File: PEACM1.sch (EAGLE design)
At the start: 15 parts

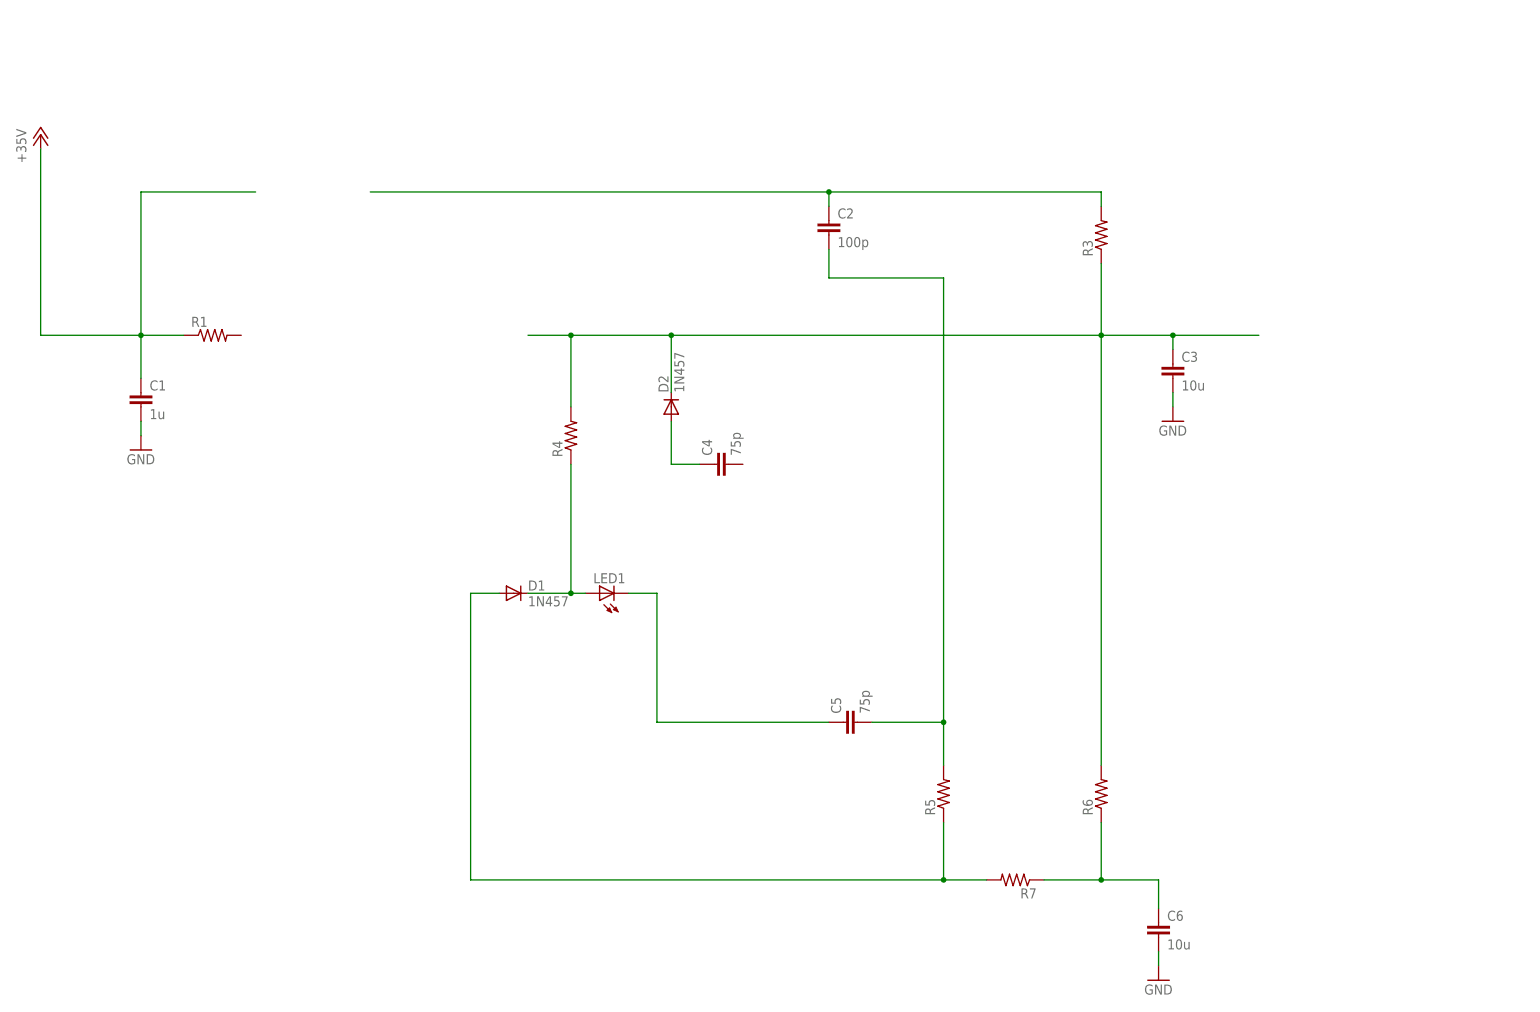
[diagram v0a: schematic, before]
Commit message: Schematic components from example complete. Needs connectors, V+ for OpAmp.
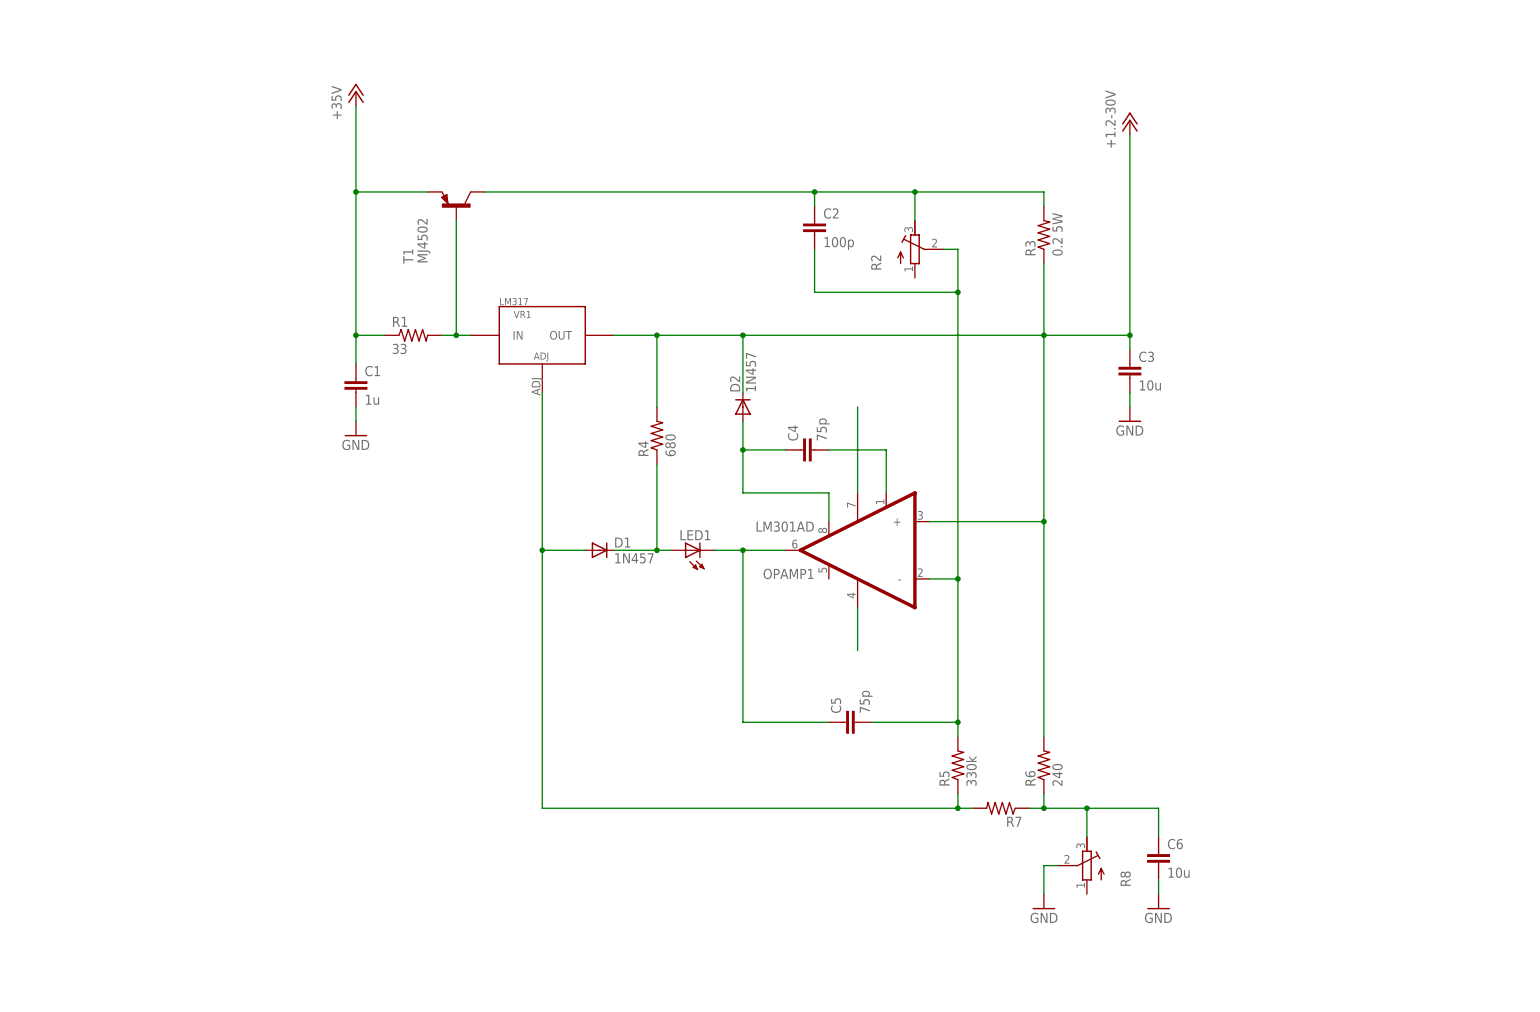
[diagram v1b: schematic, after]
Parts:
- added OPAMP1: LM301AD, PEAC:LM301AD
- added R2, R8: (no value), rcl:R-TRIMM4G/J
- added T1: MJ4502, transistor:-PNP-TO3
- added VR1: LM317, PEAC:LM317
- R1: value (none) -> 33
- R3: value (none) -> 0.2 5W; device rcl:R-US_M1206 -> rcl:R-US_R4527
- R4: value (none) -> 680
- R5: value (none) -> 330k
- R6: value (none) -> 240
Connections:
- new net +1.2-30V: C3.1, D2.C, OPAMP1.+@3, R3.1, R4.2, R6.2, VR1.OUT
- new net N$1: C4.2, OPAMP1.BAL#1
- new net VCC+@7: OPAMP1.VCC+@7
- new net VCC-@4: OPAMP1.VCC-@4
- net +35V: now also T1.E
- net GND: now also R8.S
- net N$11: now also OPAMP1.OUT_A@6
- net N$2: now also R2.E, T1.C
- net N$3: now also R1.2, T1.B, VR1.IN; no longer C3.1, D2.C, R3.1, R4.2, R6.2
- net N$4: now also OPAMP1.-@2, R2.S
- net N$5: now also VR1.ADJ
- net N$6: now also R8.E
- net N$9: now also OPAMP1.BAL@8
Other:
- moved on the sheet: C1, C2, C3, C4, C6, D1, D2, LED1, R1, R3, R4, R5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

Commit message: Schematic and layout ready for review.
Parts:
- added H1, H2: MOUNT-PAD-ROUND2.8, holes:MOUNT-PAD-ROUND2.8
- added JP1, JP2: (no value), pinhead:PINHD-1X2
- added R9: NU, rcl:R-US_M1206
- R7: value (none) -> 220
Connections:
- removed net VCC+@7: OPAMP1.VCC+@7
- removed net VCC-@4: OPAMP1.VCC-@4
- new net VCC-: OPAMP1.VCC-@4, R9.2
- net +1.2-30V: now also JP2.1
- net +35V: now also JP1.2, OPAMP1.VCC+@7
- net GND: now also H1.MOUNT, H2.MOUNT, JP1.1, JP2.2, R9.1
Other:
- moved on the sheet: C5, C6, R5, R6, R7, R8

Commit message: Completed board layout.
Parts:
- added JP3: (no value), pinhead:PINHD-1X2
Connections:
- net GND: now also JP3.1
- net VCC-: now also JP3.2
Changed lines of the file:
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@@
 <part name="H2" library="holes" deviceset="MOUNT-PAD-ROUND" device="2.8"/>
 <part name="GND8" library="PEAC" deviceset="GND" device=""/>
+<part name="JP3" library="pinhead" deviceset="PINHD-1X2" device=""/>
+<part name="GND9" library="PEAC" deviceset="GND" device=""/>
 </parts>
 <sheets>
@@
 <instance part="H2" gate="G$1" x="312.42" y="106.68"/>
 <instance part="GND8" gate="1" x="304.8" y="96.52"/>
+<instance part="JP3" gate="G$1" x="195.58" y="91.44" rot="R180"/>
+<instance part="GND9" gate="1" x="205.74" y="63.5" rot="MR0"/>
 </instances>
 <busses>
@@
 <wire x1="309.88" y1="106.68" x2="304.8" y2="106.68" width="0.1524" layer="91"/>
 <junction x="304.8" y="106.68"/>
+</segment>
+<segment>
+<pinref part="JP3" gate="G$1" pin="1"/>
+<wire x1="198.12" y1="88.9" x2="205.74" y2="88.9" width="0.1524" layer="91"/>
+<wire x1="205.74" y1="88.9" x2="205.74" y2="66.04" width="0.1524" layer="91"/>
+<pinref part="GND9" gate="1" pin="GND"/>
 </segment>
 </net>
@@
 <segment>
 <pinref part="OPAMP1" gate="G$1" pin="VCC-@4"/>
-<wire x1="228.6" y1="104.14" x2="228.6" y2="93.98" width="0.1524" layer="91"/>
+<wire x1="228.6" y1="104.14" x2="228.6" y2="96.52" width="0.1524" layer="91"/>
 <pinref part="R9" gate="G$1" pin="2"/>
-</segment>
-</net>
+<wire x1="228.6" y1="96.52" x2="228.6" y2="93.98" width="0.1524" layer="91"/>
+<wire x1="228.6" y1="96.52" x2="223.52" y2="96.52" width="0.1524" layer="91"/>
+<wire x1="223.52" y1="96.52" x2="223.52" y2="91.44" width="0.1524" layer="91"/>
+<junction x="228.6" y="96.52"/>
+<pinref part="JP3" gate="G$1" pin="2"/>
+<wire x1="223.52" y1="91.44" x2="198.12" y2="91.44" width="0.1524" layer="91"/>
+</segment>
+</net>

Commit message: Added -6V regulator, banana jacks.
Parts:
- removed JP1, JP2, JP3: (no value), pinhead:PINHD-1X2
- added C7, C8: 1u, rcl:C-EUC0805
- added H3, H4: MOUNT-PAD-ROUND2.8, holes:MOUNT-PAD-ROUND2.8
- added J1, J2: BU-P2269, PEAC:BU-P2269
- added R10: 10, rcl:R-US_R1206
- added R11: 33, rcl:R-US_M1206
- added SD2: STPS0540Z, motorFeedback:STPS0540Z
- added VR2: LM337, PEAC:LM337
- R2: value (none) -> 250k
- R9: value NU -> 33
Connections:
- net N$2 renamed EMITTER_RES
- new net N$2: C7.1, R11.2, SD2.C
- new net N$7: C6.1, R10.2, R6.1, R7.1
- new net SCH_RES_VCC-: R11.1, R9.2, VR2.ADJ
- net +1.2-30V: now also J2.+; no longer JP2.1
- net +35V: now also J1.+, SD2.A; no longer JP1.2
- net GND: now also C7.2, C8.2, H3.MOUNT, H4.MOUNT, J1.-, J2.-, VR2.IN; no longer JP1.1, JP2.2, JP3.1, R9.1
- net N$6: now also R10.1; no longer C6.1, R6.1, R7.1
- net VCC-: now also C8.1, R9.1, VR2.OUT; no longer JP3.2, R9.2
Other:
- moved on the sheet: R8, R9
